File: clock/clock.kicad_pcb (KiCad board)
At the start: 2 copper layers, 145.4 x 95.5 mm, 63 parts, among them J1 Barrel_Jack, SW1 SW_Clock, SW2 CLK_SEL, SW3 SW_Step, SW4 SW_MANUAL_CLK, U1 LM7805, U10 LM555, U2 74LS93, U3 LM556, U4 74LS151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

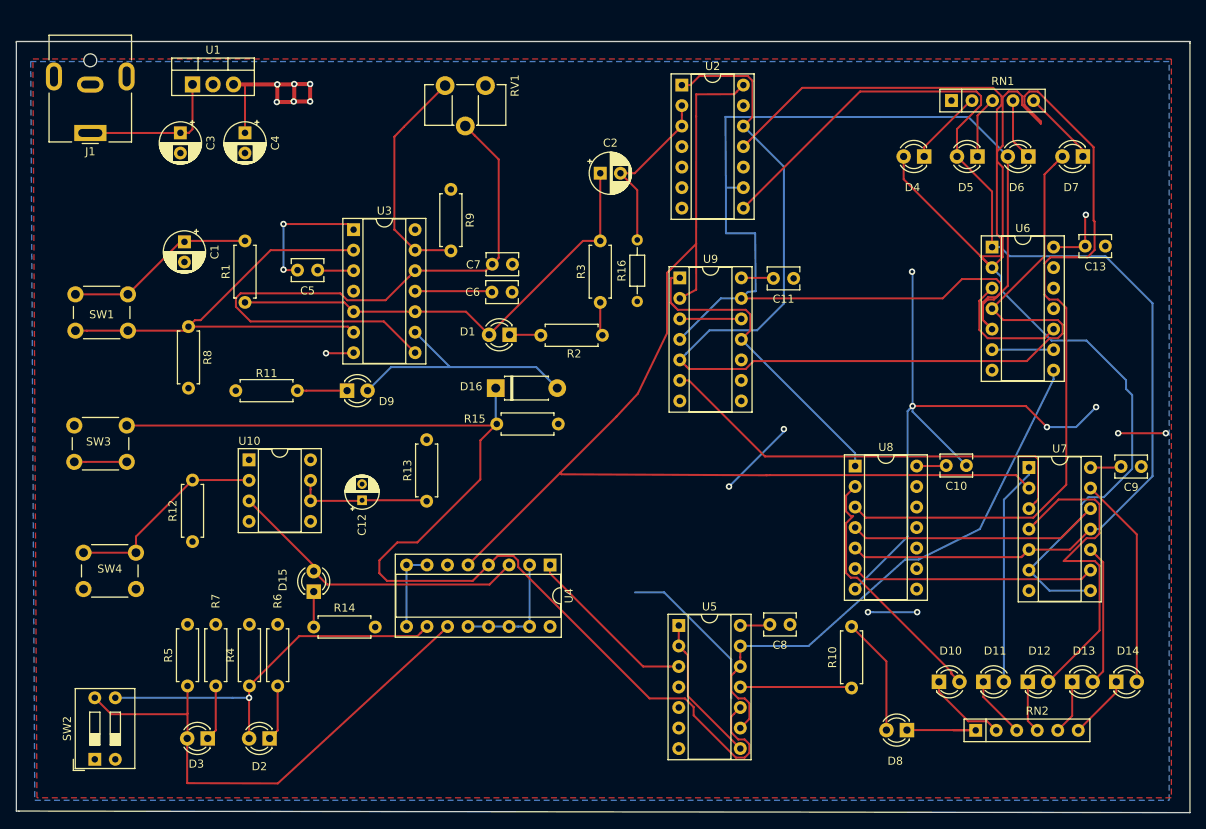
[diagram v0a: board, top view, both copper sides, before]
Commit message: Added switches and redesign
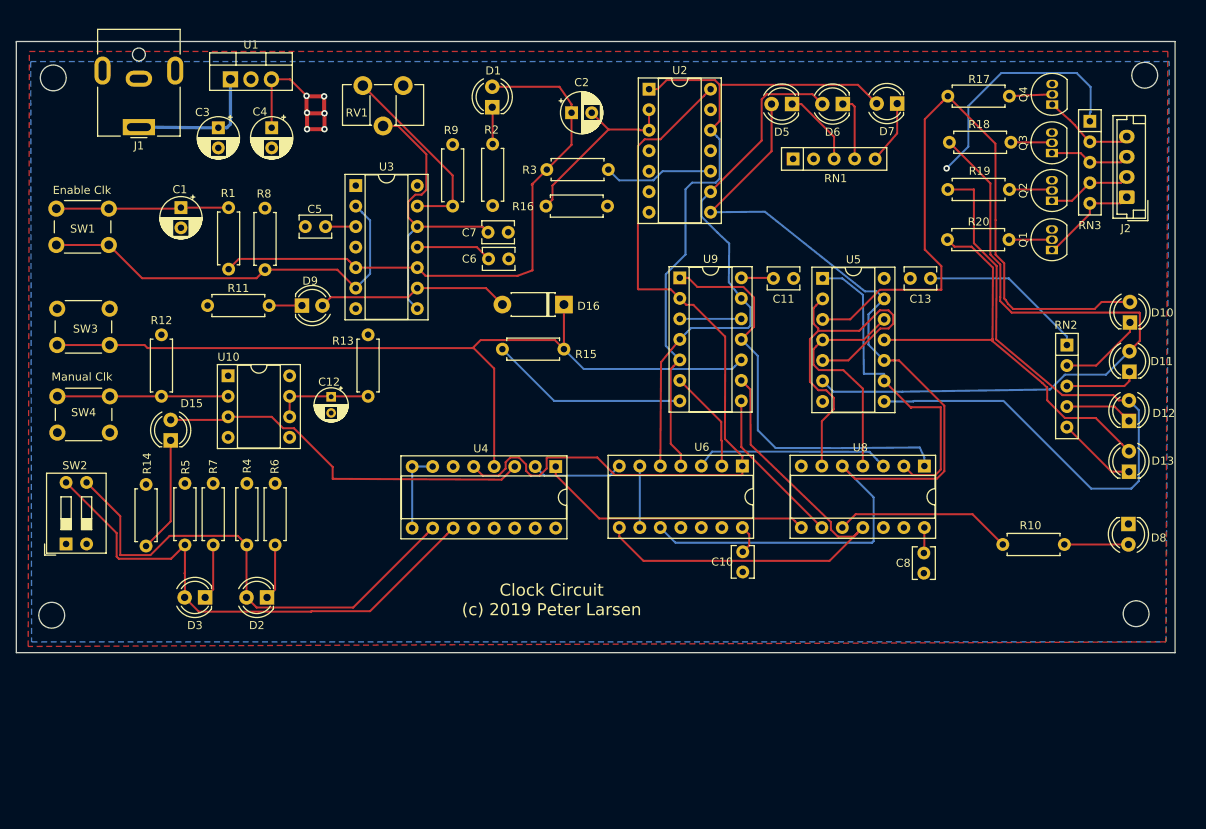
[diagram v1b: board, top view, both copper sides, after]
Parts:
- removed C9: 10pF, Capacitor_THT:C_Disc_D3.8mm_W2.6mm_P2.50mm
- removed D14, D4: LED_Small, LED_THT:LED_D3.0mm
- removed U7: 74LS02, Package_DIP:DIP-14_W7.62mm_Socket
- added J2: Conn_01x04, Connector_JST:JST_EH_B4B-EH-A_1x04_P2.50mm_Vertical, F.Cu at (199.8, 82.3)
- added Q1: 2N3904, Package_TO_SOT_THT:TO-92_Inline, F.Cu at (190.6, 88.9)
- added Q2: 2N3904, Package_TO_SOT_THT:TO-92_Inline, F.Cu at (190.6, 82.8)
- added Q3: 2N3904, Package_TO_SOT_THT:TO-92_Inline, F.Cu at (190.6, 76.9)
- added Q4: 2N3904, Package_TO_SOT_THT:TO-92_Inline, F.Cu at (190.6, 70.9)
- added R17: 1K, Resistor_THT:R_Axial_DIN0207_L6.3mm_D2.5mm_P7.62mm_Horizontal, F.Cu at (185.3, 69.8)
- added R18: 1K, Resistor_THT:R_Axial_DIN0207_L6.3mm_D2.5mm_P7.62mm_Horizontal, F.Cu at (185.5, 75.5)
- added R19: 1K, Resistor_THT:R_Axial_DIN0207_L6.3mm_D2.5mm_P7.62mm_Horizontal, F.Cu at (185.3, 81.4)
- added R20: 1K, Resistor_THT:R_Axial_DIN0207_L6.3mm_D2.5mm_P7.62mm_Horizontal, F.Cu at (185.2, 87.6)
- added REF**: MountingHole_3.2mm_M3, MountingHole:MountingHole_3.2mm_M3, F.Cu at (202.0, 67.2)
- added REF**: MountingHole_3.2mm_M3, MountingHole:MountingHole_3.2mm_M3, F.Cu at (201.0, 133.9)
- added REF**: MountingHole_3.2mm_M3, MountingHole:MountingHole_3.2mm_M3, F.Cu at (66.7, 134.1)
- added REF**: MountingHole_3.2mm_M3, MountingHole:MountingHole_3.2mm_M3, F.Cu at (66.9, 67.6)
- added RN3: 10K, Resistor_THT:R_Array_SIP5, F.Cu at (195.2, 72.9)
- D1, D10, D11, D12, D13, D15, D2, D3, D5, D6, D7, D8, D9: footprint LED_THT:LED_D3.0mm -> LED_THT:LED_D4.0mm
- R16: footprint Resistor_THT:R_Axial_DIN0204_L3.6mm_D1.6mm_P7.62mm_Horizontal -> Resistor_THT:R_Axial_DIN0207_L6.3mm_D2.5mm_P7.62mm_Horizontal
- RN1: value R_Network04 -> 470
- RN2: footprint Resistor_THT:R_Array_SIP6 -> Resistor_THT:R_Array_SIP5
- SW1: value SW_Clock -> Enable Clk
- SW3: value SW_Step -> Step
- SW4: value SW_MANUAL_CLK -> Manual Clk
- U5: value 74LS00 -> 74LS08
- moved D10 50.4 mm to (200.2, 97.9), turned to 90 degrees
- moved RN2 49.0 mm to (192.4, 100.6), turned to 270 degrees
- moved U5 46.5 mm to (162.2, 92.4)
- moved D11 42.5 mm to (200.2, 103.9), turned to 90 degrees
- moved U6 41.1 mm to (152.2, 115.6), turned to 270 degrees
- moved D8 37.5 mm to (200.0, 122.8), turned to 270 degrees
- moved D12 34.7 mm to (200.1, 110.0), turned to 90 degrees
- moved C10 30.7 mm to (152.3, 128.8), turned to 90 degrees
- moved D1 28.3 mm to (121.2, 71.2), turned to 90 degrees
- moved D13 27.0 mm to (200.1, 116.3), turned to 90 degrees
- moved SW2 26.9 mm to (68.5, 125.3)
- moved R10 25.8 mm to (184.5, 125.3), turned to 0 degrees
- moved D15 25.8 mm to (81.4, 112.5)
- moved R2 24.4 mm to (121.3, 75.8), turned to 270 degrees
- moved D7 23.9 mm to (171.4, 70.7)
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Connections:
- U2 pad 11: PUL3 -> Net-(U2-Pad11)
- U5 pad 10: AFREQ -> PUL2
- U5 pad 11: Net-(R10-Pad1) -> Net-(D13-Pad2)
- U5 pad 13: Net-(U5-Pad12) -> PUL2
- U5 pad 2: Net-(U5-Pad1) -> Net-(U5-Pad2)
- U5 pad 3: STEP -> Net-(D10-Pad2)
- U5 pad 4: (no net) -> Net-(U5-Pad12)
- U5 pad 5: (no net) -> Net-(U5-Pad2)
- U5 pad 6: (no net) -> Net-(D11-Pad2)
- U5 pad 8: Net-(U5-Pad1) -> Net-(D12-Pad2)
- U5 pad 9: Net-(U5-Pad12) -> Net-(U5-Pad1)
- U6 pad 1: PUL2 -> CLK
- U6 pad 10: Net-(U6-Pad10) -> PUL2
- U6 pad 2: PUL3 -> Net-(U6-Pad2)
- U6 pad 3: Net-(U6-Pad10) -> Net-(U6-Pad3)
- U6 pad 8: Net-(U5-Pad12) -> Net-(U6-Pad8)
- U8 pad 10: (no net) -> Net-(R10-Pad1)
- U8 pad 11: (no net) -> Net-(U6-Pad8)
- U8 pad 2: Net-(D10-Pad2) -> Net-(U5-Pad1)
- U8 pad 3: PUL3 -> Net-(U6-Pad3)
- U8 pad 4: Net-(U7-Pad12) -> Net-(U5-Pad12)
- U8 pad 6: Net-(U7-Pad9) -> Net-(U5-Pad2)
- U8 pad 8: (no net) -> STEP
- U8 pad 9: (no net) -> Net-(U8-Pad9)
- U9 pad 10: (no net) -> AFREQ
- U9 pad 6: Net-(U7-Pad3) -> Net-(U6-Pad2)
- U9 pad 8: (no net) -> Net-(U8-Pad9)
- U9 pad 9: (no net) -> Net-(U6-Pad8)
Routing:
- net PUL3: track 263.4 -> 0.00 mm
- net PUL1: track 140.8 -> 67.8 mm
- net Net-(U6-Pad8): track 0.00 -> 62.2 mm
- net Net-(D10-Pad2): track 31.8 -> 90.0 mm
- net Net-(D11-Pad2): track 27.8 -> 86.0 mm
- net Net-(U7-Pad3): track 55.0 -> 0.00 mm
- net PUL0: track 138.2 -> 84.2 mm
- net Net-(D12-Pad2): track 41.7 -> 89.1 mm
- net Net-(U5-Pad2): track 0.00 -> 46.5 mm
- net CLK: track 143.1 -> 100.0 mm
- net GND: track 154.0 -> 111.4 mm, vias 11 -> 1
- net ATHR: track 79.0 -> 37.8 mm
- net Net-(U5-Pad12): track 68.9 -> 29.1 mm
- net Net-(D13-Pad2): track 17.6 -> 52.8 mm
- net AFREQ: track 143.0 -> 108.6 mm
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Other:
- board size 145.4 x 95.5 mm -> 143.5 x 75.7 mm
- board text added: "Clock Circuit (c) 2019 Peter Larsen"

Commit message: Reduced/condensed size - added mounting holes
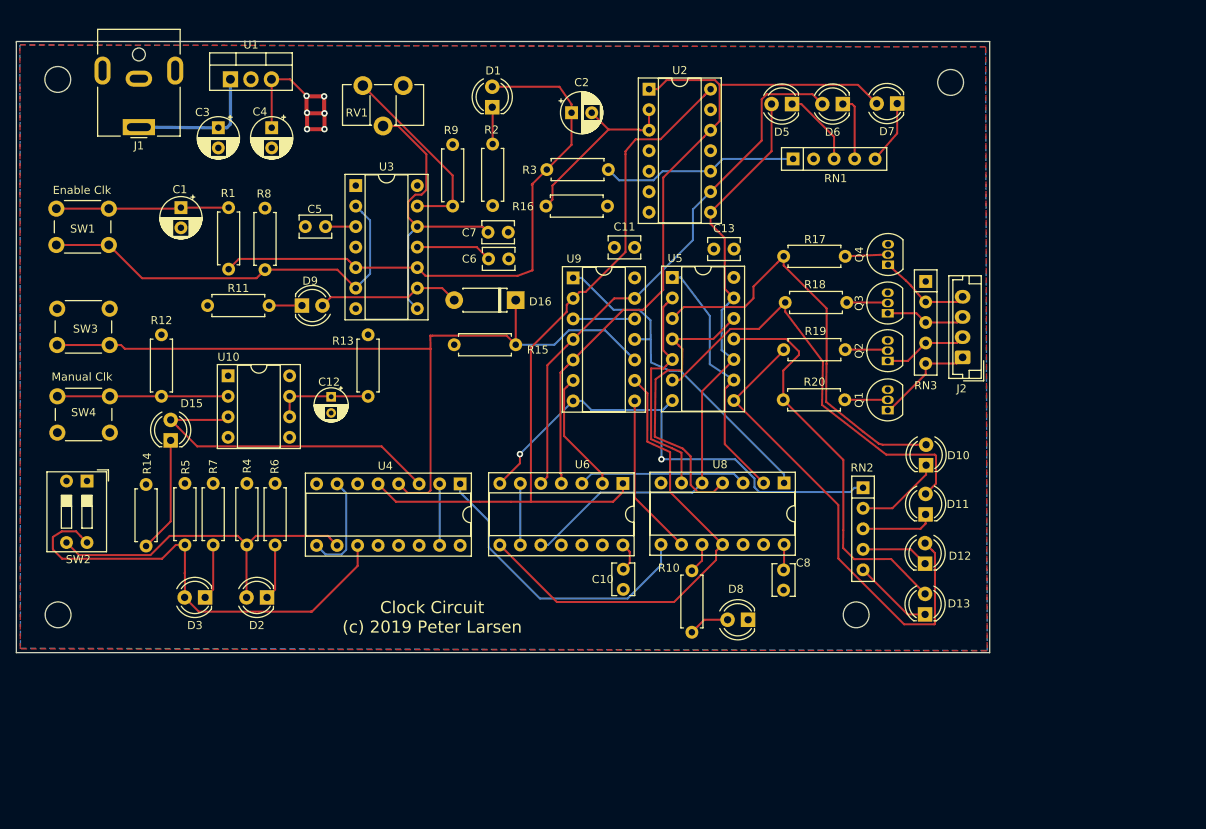
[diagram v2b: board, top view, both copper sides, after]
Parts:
- moved D8 48.6 mm to (152.9, 134.7), turned to 180 degrees
- moved R10 38.6 mm to (146.0, 128.6), turned to 270 degrees
- moved REF** 34.7 mm to (166.3, 134.1)
- moved D13 30.8 mm to (174.8, 134.0)
- moved RN2 30.8 mm to (167.2, 118.3)
- moved D10 30.8 mm to (175.0, 115.5)
- moved D12 30.8 mm to (174.8, 127.7)
- moved D11 30.8 mm to (174.9, 121.6)
- moved Q1 28.4 mm to (170.2, 108.7)
- moved Q2 28.4 mm to (170.2, 102.6)
- moved Q3 28.4 mm to (170.2, 96.7)
- moved R17 28.4 mm to (164.9, 89.7)
- moved R19 28.4 mm to (164.9, 101.2)
- moved Q4 28.4 mm to (170.3, 90.7)
- moved R18 28.4 mm to (165.1, 95.4)
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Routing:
- net PUL2: track 120.9 -> 77.4 mm
- net Net-(D10-Pad2): track 90.0 -> 52.3 mm
- net Net-(D11-Pad2): track 86.0 -> 53.8 mm
- net Net-(D12-Pad2): track 89.1 -> 59.7 mm
- net Net-(D2-Pad2): track 62.0 -> 43.1 mm
- net Net-(R10-Pad1): track 22.1 -> 3.77 mm
- net Net-(U5-Pad2): track 46.5 -> 28.3 mm
- net Net-(U8-Pad1): track 51.5 -> 42.0 mm
- net Net-(U5-Pad1): track 40.3 -> 31.8 mm
- net Net-(U5-Pad12): track 29.1 -> 37.3 mm
- net Net-(D3-Pad2): track 66.0 -> 57.8 mm
- net Net-(D16-Pad2): track 24.0 -> 17.8 mm
- net MFREQ: track 47.5 -> 41.3 mm
- net AFREQ: track 108.6 -> 103.7 mm
- net PUL0: track 84.2 -> 88.9 mm
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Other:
- board size 143.5 x 75.7 mm -> 120.5 x 75.7 mm

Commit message: Fixed plug sizes and foot prints
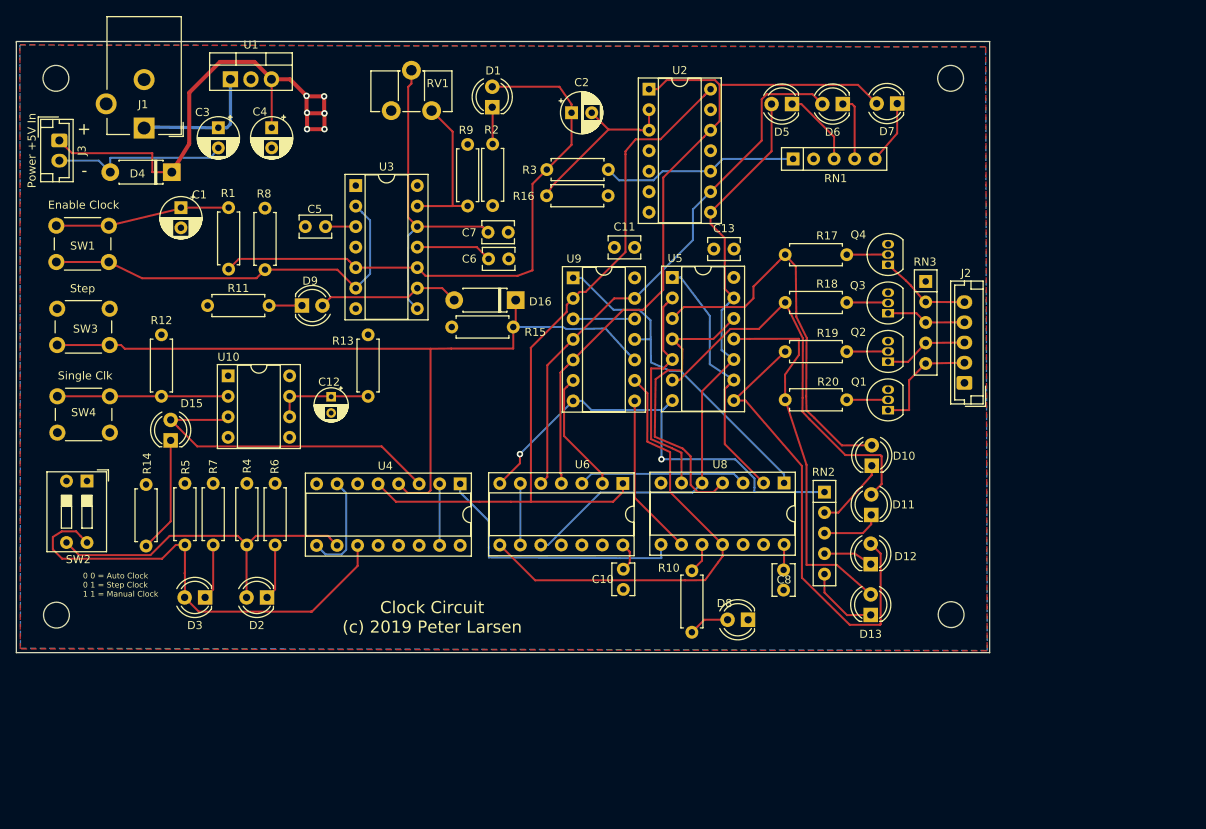
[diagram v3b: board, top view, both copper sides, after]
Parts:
- added D4: D, Diode_THT:D_DO-41_SOD81_P7.62mm_Horizontal, F.Cu at (81.5, 79.2)
- added J3: Power +5V In, Connector_JST:JST_EH_B2B-EH-A_1x02_P2.50mm_Vertical, F.Cu at (67.6, 75.3)
- J1: footprint Connector_BarrelJack:BarrelJack_CUI_PJ-063AH_Horizontal -> Connector_BarrelJack:BarrelJack_CUI_PJ-102AH_Horizontal
- J2: footprint Connector_JST:JST_EH_B4B-EH-A_1x04_P2.50mm_Vertical -> Connector_JST:JST_EH_B5B-EH-A_1x05_P2.50mm_Vertical
- SW1: value Enable Clk -> SW_Clock
- SW3: value Step -> SW_Step
- SW4: value Manual Clk -> SW_MANUAL_CLK
- moved REF** 11.8 mm to (178.1, 134.0)
- moved D11 6.73 mm to (168.2, 121.7)
- moved D10 6.73 mm to (168.2, 115.6)
- moved D12 6.73 mm to (168.1, 127.8)
- moved D13 6.73 mm to (168.1, 134.1)
- moved RN2 4.80 mm to (162.4, 118.9)
- moved RV1 3.44 mm to (108.7, 71.6), turned to 90 degrees
- moved J2 3.17 mm to (179.7, 105.3)
- moved R15 2.22 mm to (123.8, 98.4)
- moved SW1 2.11 mm to (67.2, 85.9)
- moved R9 1.85 mm to (118.2, 75.8)
- moved R16 1.28 mm to (135.6, 82.2)
- moved J1 0.66 mm to (78.1, 73.8)
- moved REF** 0.51 mm to (178.0, 67.6)
- moved R19 0.31 mm to (165.1, 101.5)
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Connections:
- J2 pad 1: Net-(J2-Pad1) -> GND
- Q1 pad 1: Net-(J2-Pad1) -> Net-(J2-Pad2)
- Q2 pad 1: Net-(J2-Pad2) -> Net-(J2-Pad3)
- Q3 pad 1: Net-(J2-Pad3) -> Net-(J2-Pad4)
- Q4 pad 1: Net-(J2-Pad4) -> Net-(J2-Pad5)
- RN3 pad 2: Net-(J2-Pad4) -> Net-(J2-Pad5)
- RN3 pad 3: Net-(J2-Pad3) -> Net-(J2-Pad4)
- RN3 pad 4: Net-(J2-Pad2) -> Net-(J2-Pad3)
- RN3 pad 5: Net-(J2-Pad1) -> Net-(J2-Pad2)
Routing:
- net +5V: track 32.9 -> 72.9 mm
- net GND: track 107.7 -> 125.8 mm
- net Net-(J2-Pad1): track 12.7 -> 0.00 mm
- net Net-(J2-Pad5): track 0.00 -> 11.4 mm
- net Net-(R9-Pad2): track 23.9 -> 19.1 mm
- net Net-(D11-Pad2): track 53.8 -> 49.5 mm
- net Net-(D10-Pad2): track 52.3 -> 48.1 mm
- net STEP: track 37.6 -> 33.6 mm
- net Net-(J2-Pad2): track 10.6 -> 14.1 mm
- net Net-(D13-Pad2): track 49.5 -> 46.3 mm
- net ATHR: track 37.8 -> 40.2 mm
- net Net-(D12-Pad1): track 8.42 -> 6.12 mm
- net Net-(D12-Pad2): track 59.7 -> 57.4 mm
- net AFREQ: track 103.7 -> 101.7 mm
- net Net-(U6-Pad8): track 59.6 -> 57.8 mm
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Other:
- board text added: "+"
- board text added: "-"
- board text added: "0 0 = Auto Clock 0 1 = Step Clock 1 1 = Manual Clock"

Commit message: Corrected LM556 toggle switch circuit
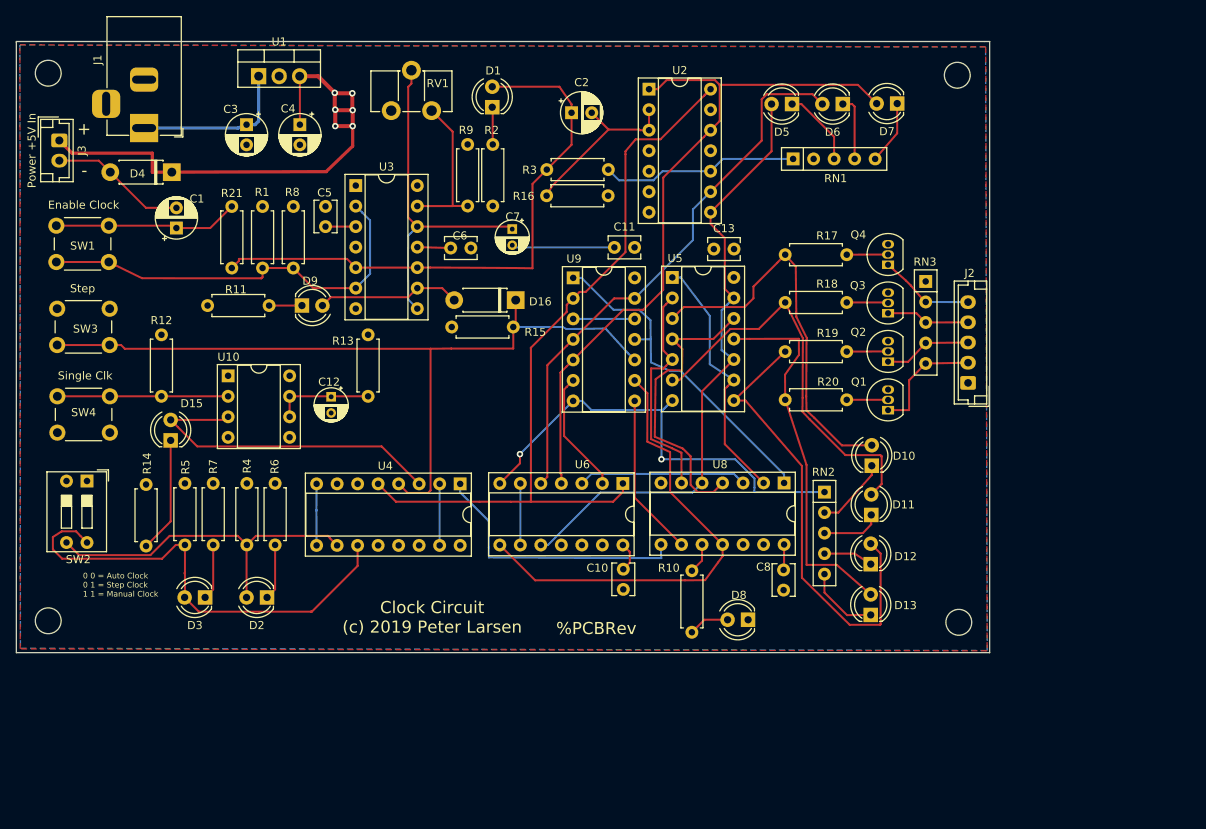
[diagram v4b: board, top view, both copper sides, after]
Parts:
- removed the REF** at (178.0, 67.6)
- removed the REF** at (178.1, 134.0)
- removed the REF** at (67.3, 134.1)
- removed the REF** at (67.2, 67.6)
- added R21: 100K, Resistor_THT:R_Axial_DIN0207_L6.3mm_D2.5mm_P7.62mm_Horizontal, F.Cu at (89.0, 91.1)
- added REF**: MountingHole_3.2mm_M3, MountingHole:MountingHole_3.2mm_M3, F.Cu at (178.8, 67.2)
- added REF**: MountingHole_3.2mm_M3, MountingHole:MountingHole_3.2mm_M3, F.Cu at (179.0, 135.0)
- added REF**: MountingHole_3.2mm_M3, MountingHole:MountingHole_3.2mm_M3, F.Cu at (66.2, 134.8)
- added REF**: MountingHole_3.2mm_M3, MountingHole:MountingHole_3.2mm_M3, F.Cu at (66.2, 67.0)
- C7: footprint Capacitor_THT:C_Disc_D3.8mm_W2.6mm_P2.50mm -> Capacitor_THT:CP_Radial_D4.0mm_P2.00mm
- J1: footprint Connector_BarrelJack:BarrelJack_CUI_PJ-102AH_Horizontal -> Connector_BarrelJack:BarrelJack_Horizontal
- moved C6 4.88 mm to (116.1, 88.6)
- moved R1 4.21 mm to (92.8, 91.1)
- moved C4 3.51 mm to (97.4, 73.4)
- moved C3 3.51 mm to (90.8, 73.4)
- moved U1 3.51 mm to (92.3, 67.4)
- moved R8 3.51 mm to (96.6, 91.1)
- moved C7 3.02 mm to (123.7, 86.3), turned to 270 degrees
- moved C1 2.59 mm to (82.1, 86.2), turned to 90 degrees
- moved J2 0.44 mm to (180.2, 105.3)
- moved R2 0.05 mm to (121.3, 75.8)
- turned C5 to 90 degrees
- turned J1 to 270 degrees
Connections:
- R1 pad 1: AEN -> BTHR
- R1 pad 2: Net-(C1-Pad1) -> +5V
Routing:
- net Net-(C6-Pad1): track 9.43 -> 4.14 mm
- net VCC: track 16.2 -> 20.0 mm
- net +5V: track 72.9 -> 75.9 mm
- net ATHR: track 40.2 -> 43.0 mm
- net GND: track 125.8 -> 127.5 mm
- net Net-(C1-Pad1): track 21.6 -> 23.0 mm
- net AEN: track 72.7 -> 71.6 mm
- net BTHR: track 50.6 -> 51.4 mm
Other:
- board text added: "%PCBRev"
